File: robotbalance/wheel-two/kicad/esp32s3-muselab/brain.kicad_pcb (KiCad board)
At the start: 2 copper layers, 30.5 x 58.4 mm, 0 parts

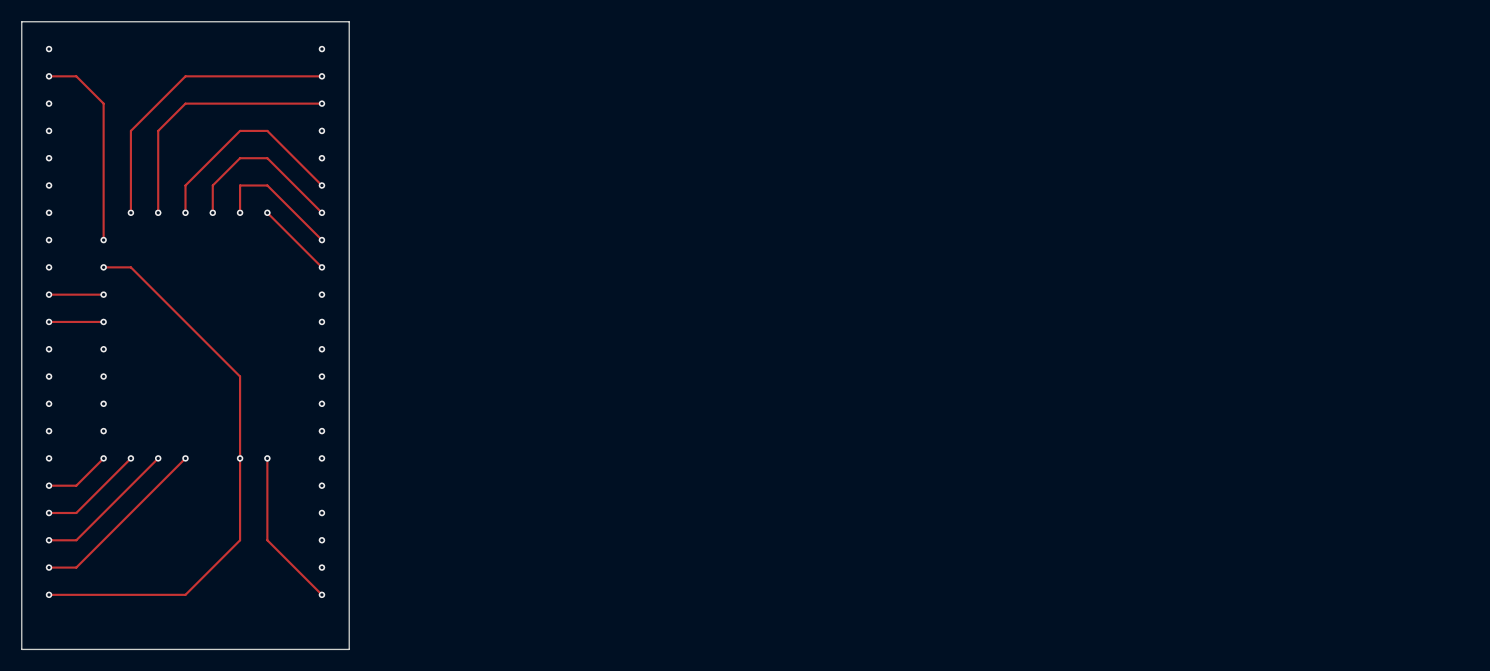
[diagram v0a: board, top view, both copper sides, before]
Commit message: balancing robot: wifi set mahony pid, modify 3d and pcb
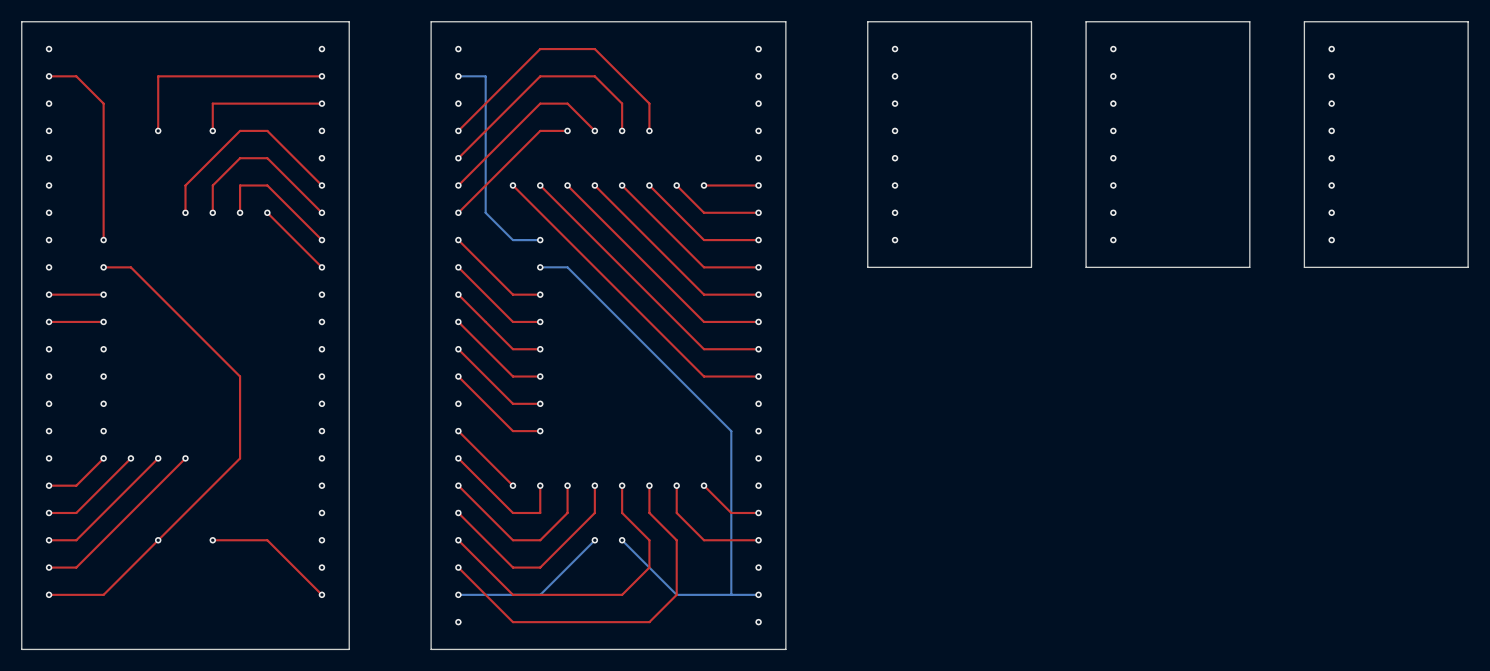
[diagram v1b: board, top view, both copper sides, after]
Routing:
- net (no net): track 248.1 -> 726.7 mm, vias 62 -> 160
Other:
- board size 30.5 x 58.4 mm -> 134.6 x 58.4 mm
- board text added: "ad0/miso"
- board text added: "bmi270"
- board text added: "cs"
- board text added: "esp32s3_muselab"
- board text added: "esp32s3_weact"
- board text added: "icm42688"
- board text added: "int1"
- board text added: "int2"
- board text added: "mpu6050"
- board text added: "scl/sclk"
- board text added: "sda/mosi"

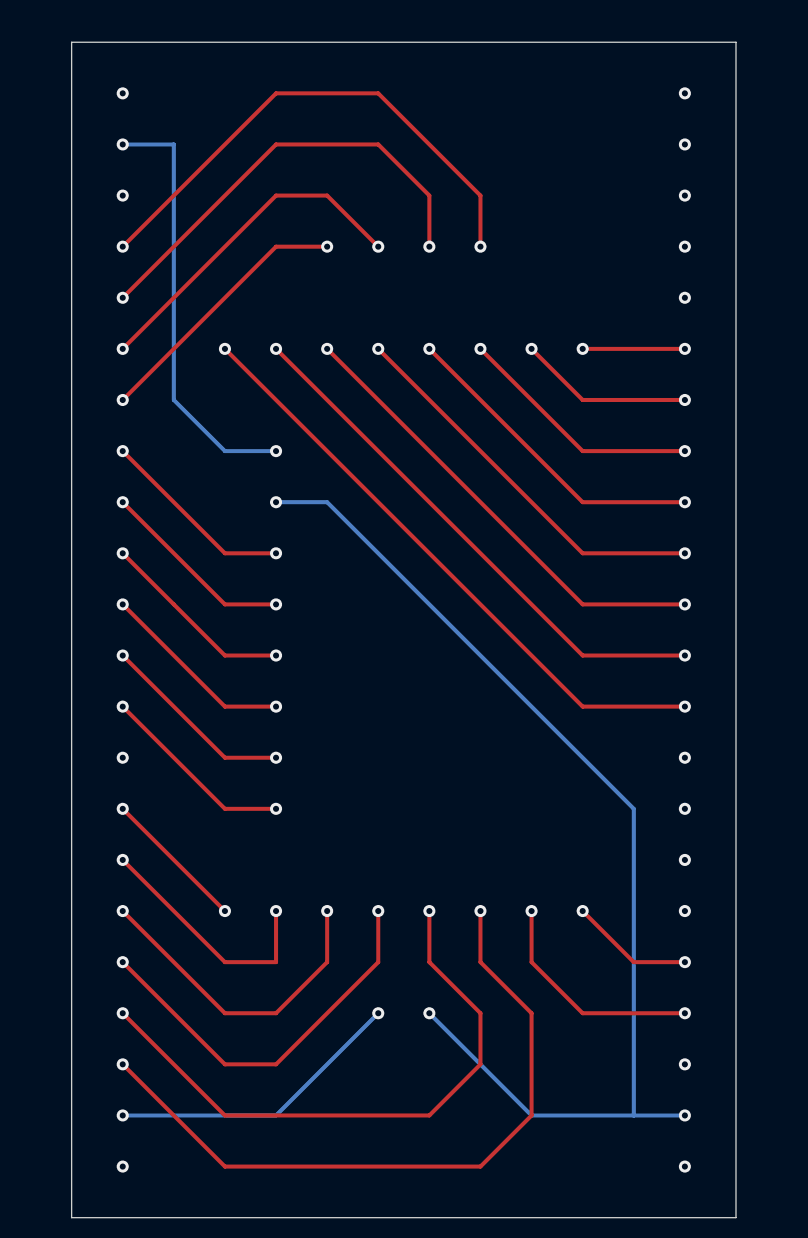
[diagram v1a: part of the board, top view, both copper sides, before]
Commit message: balancing robot: 1.change pid in web in wifi 2.power board 3.another logic board esp32s3_weact+icm42688
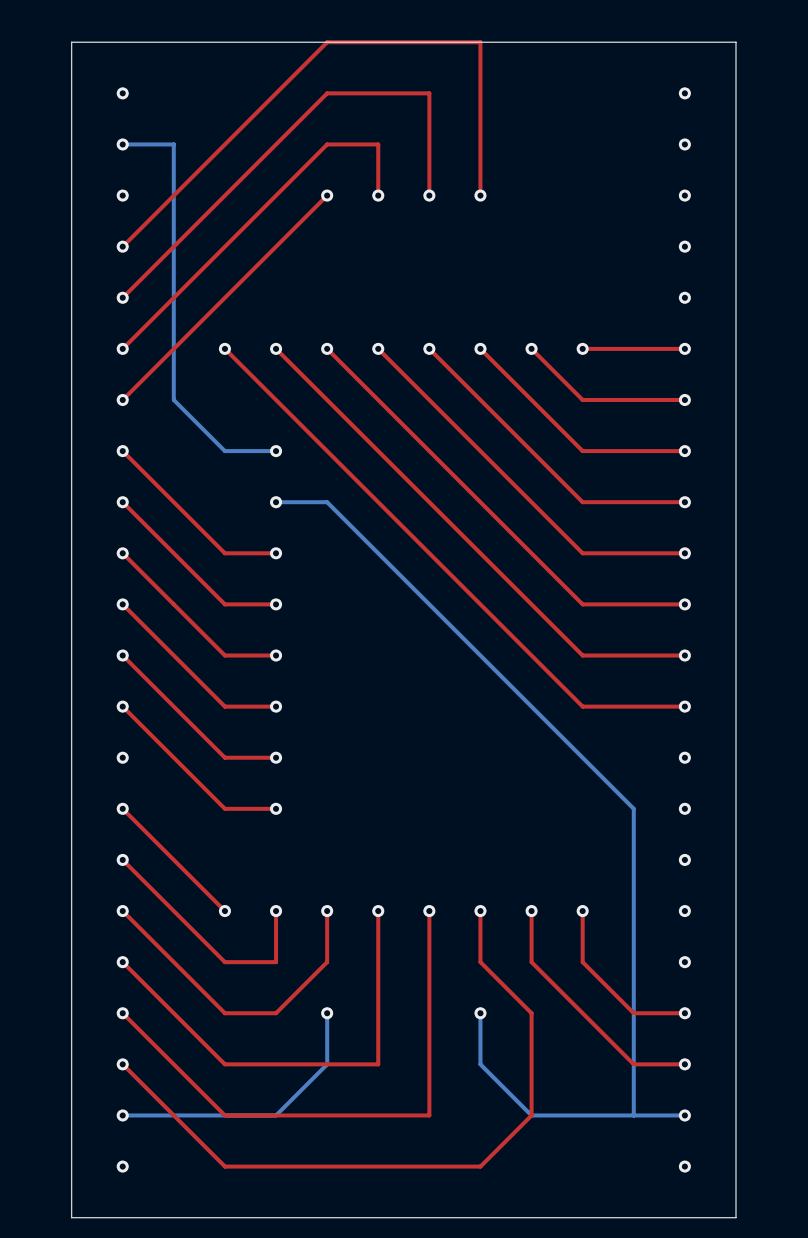
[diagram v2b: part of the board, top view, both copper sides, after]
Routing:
- net (no net): track 726.7 -> 739.3 mm

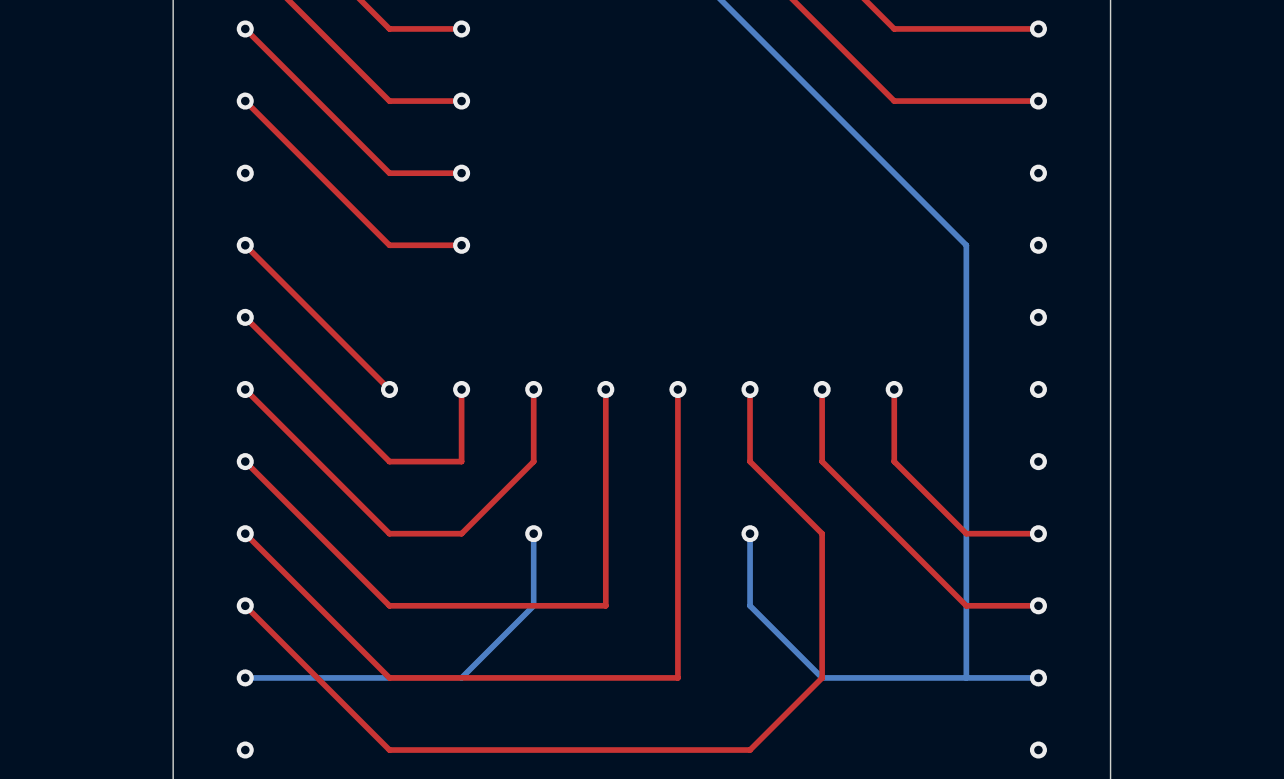
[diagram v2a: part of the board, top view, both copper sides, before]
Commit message: balancing robot stepper motor, dont use esp32s3 pin19,20(usb)
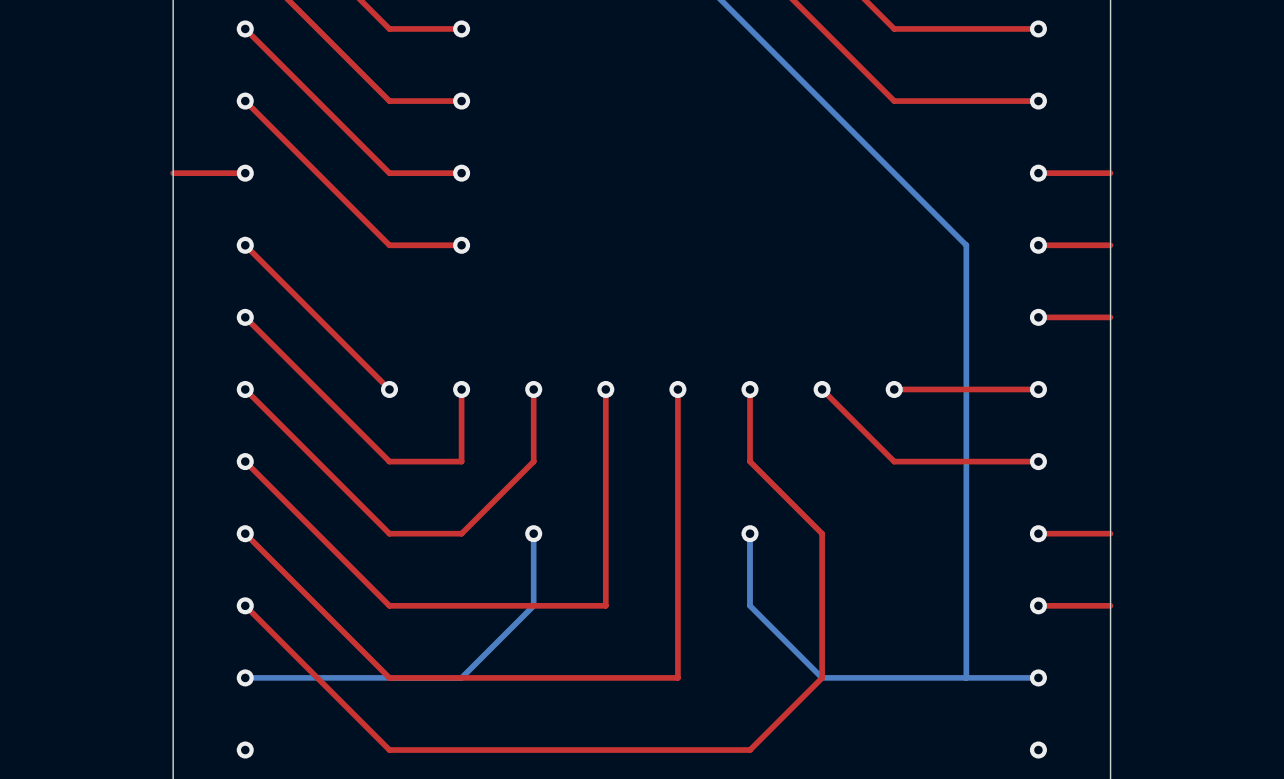
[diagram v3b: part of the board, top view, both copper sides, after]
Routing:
- net (no net): track 739.3 -> 747.3 mm
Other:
- board text added: "?"
- board text added: "boot"
- board text added: "d+"
- board text added: "d-"
- board text added: "key"
- board text added: "led"
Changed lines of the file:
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@@
 		(layer "Edge.Cuts")
+	)
+	(gr_text "d-"
+		(at 172.72 104.14 0)
+		(layer "F.Paste")
+		(effects
+			(font
+				(size 1 1)
+				(thickness 0.15)
+			)
+			(justify right bottom)
+		)
 	)
 	(gr_text "36"
@@
 		)
 	)
+	(gr_text "d+"
+		(at 172.72 101.6 0)
+		(layer "F.Paste")
+		(effects
+			(font
+				(size 1 1)
+				(thickness 0.15)
+			)
+			(justify right bottom)
+		)
+	)
 	(gr_text "scl/sclk"
 		(at 149.86 83.82 0)
@@
 		)
 	)
+	(gr_text "?"
+		(at 139.7 88.9 0)
+		(layer "F.Paste")
+		(effects
+			(font
+				(size 1 1)
+				(thickness 0.15)
+			)
+			(justify left bottom)
+		)
+	)
 	(gr_text "19"
 		(at 167.64 104.14 0)
@@
 		)
 	)
+	(gr_text "led"
+		(at 172.72 93.98 0)
+		(layer "F.Paste")
+		(effects
+			(font
+				(size 1 1)
+				(thickness 0.15)
+			)
+			(justify right bottom)
+		)
+	)
 	(gr_text "int1"
 		(at 223.52 71.12 0)
@@
 		)
 	)
+	(gr_text "boot"
+		(at 172.72 88.9 0)
+		(layer "F.Paste")
+		(effects
+			(font
+				(size 1 1)
+				(thickness 0.15)
+			)
+			(justify right bottom)
+		)
+	)
 	(gr_text "tx"
 		(at 127 63.5 0)
@@
 		)
 	)
+	(gr_text "key"
+		(at 172.72 91.44 0)
+		(layer "F.Paste")
+		(effects
+			(font
+				(size 1 1)
+				(thickness 0.15)
+			)
+			(justify right bottom)
+		)
+	)
 	(gr_text "gnd"
 		(at 149.86 76.2 0)
@@
 	)
 	(segment
-		(start 162.56 99.06)
-		(end 167.64 104.14)
-		(width 0.2)
-		(layer "F.Cu")
-		(net 0)
-	)
-	(segment
-		(start 167.64 101.6)
-		(end 170.18 101.6)
-		(width 0.2)
-		(layer "F.Cu")
-		(net 0)
-	)
-	(segment
 		(start 142.24 83.82)
 		(end 147.32 88.9)
@@
 	)
 	(segment
+		(start 162.56 96.52)
+		(end 165.1 99.06)
+		(width 0.2)
+		(layer "F.Cu")
+		(net 0)
+	)
+	(segment
 		(start 142.24 86.36)
 		(end 147.32 91.44)
@@
 	)
 	(segment
-		(start 167.64 104.14)
-		(end 170.18 104.14)
-		(width 0.2)
-		(layer "F.Cu")
-		(net 0)
-	)
-	(segment
 		(start 152.4 58.42)
 		(end 154.94 58.42)
@@
 	)
 	(segment
-		(start 165.1 96.52)
-		(end 165.1 99.06)
+		(start 142.24 88.9)
+		(end 139.7 88.9)
 		(width 0.2)
 		(layer "F.Cu")
@@
 	)
 	(segment
+		(start 170.18 93.98)
+		(end 172.72 93.98)
+		(width 0.2)
+		(layer "F.Cu")
+		(net 0)
+	)
+	(segment
 		(start 147.32 86.36)
 		(end 149.86 86.36)
@@
 	)
 	(segment
+		(start 165.1 99.06)
+		(end 170.18 99.06)
+		(width 0.2)
+		(layer "F.Cu")
+		(net 0)
+	)
+	(segment
 		(start 147.32 106.68)
 		(end 142.24 101.6)
@@
 	)
 	(segment
+		(start 170.18 104.14)
+		(end 172.72 104.14)
+		(width 0.2)
+		(layer "F.Cu")
+		(net 0)
+	)
+	(segment
 		(start 160.02 99.06)
 		(end 160.02 96.52)
@@
 	)
 	(segment
+		(start 170.18 88.9)
+		(end 172.72 88.9)
+		(width 0.2)
+		(layer "F.Cu")
+		(net 0)
+	)
+	(segment
 		(start 152.4 99.06)
 		(end 152.4 96.52)
@@
 	)
 	(segment
+		(start 170.18 91.44)
+		(end 172.72 91.44)
+		(width 0.2)
+		(layer "F.Cu")
+		(net 0)
+	)
+	(segment
+		(start 170.18 101.6)
+		(end 172.72 101.6)
+		(width 0.2)
+		(layer "F.Cu")
+		(net 0)
+	)
+	(segment
 		(start 165.1 78.74)
 		(end 154.94 68.58)
@@
 	)
 	(segment
+		(start 165.1 96.52)
+		(end 170.18 96.52)
+		(width 0.2)
+		(layer "F.Cu")
+		(net 0)
+	)
+	(segment
 		(start 147.32 78.74)
 		(end 149.86 78.74)
@@
 	)
 	(segment
-		(start 165.1 99.06)
-		(end 167.64 101.6)
-		(width 0.2)
-		(layer "F.Cu")
-		(net 0)
-	)
-	(segment
 		(start 147.32 88.9)
 		(end 149.86 88.9)
@@
 		(width 0.2)
 		(layer "F.Cu")
-		(net 0)
-	)
-	(segment
-		(start 162.56 96.52)
-		(end 162.56 99.06)
-		(width 0.2)
-		(layer "F.Cu")
